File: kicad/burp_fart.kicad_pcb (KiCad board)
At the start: 2 copper layers, 142.2 x 120 mm, 44 parts

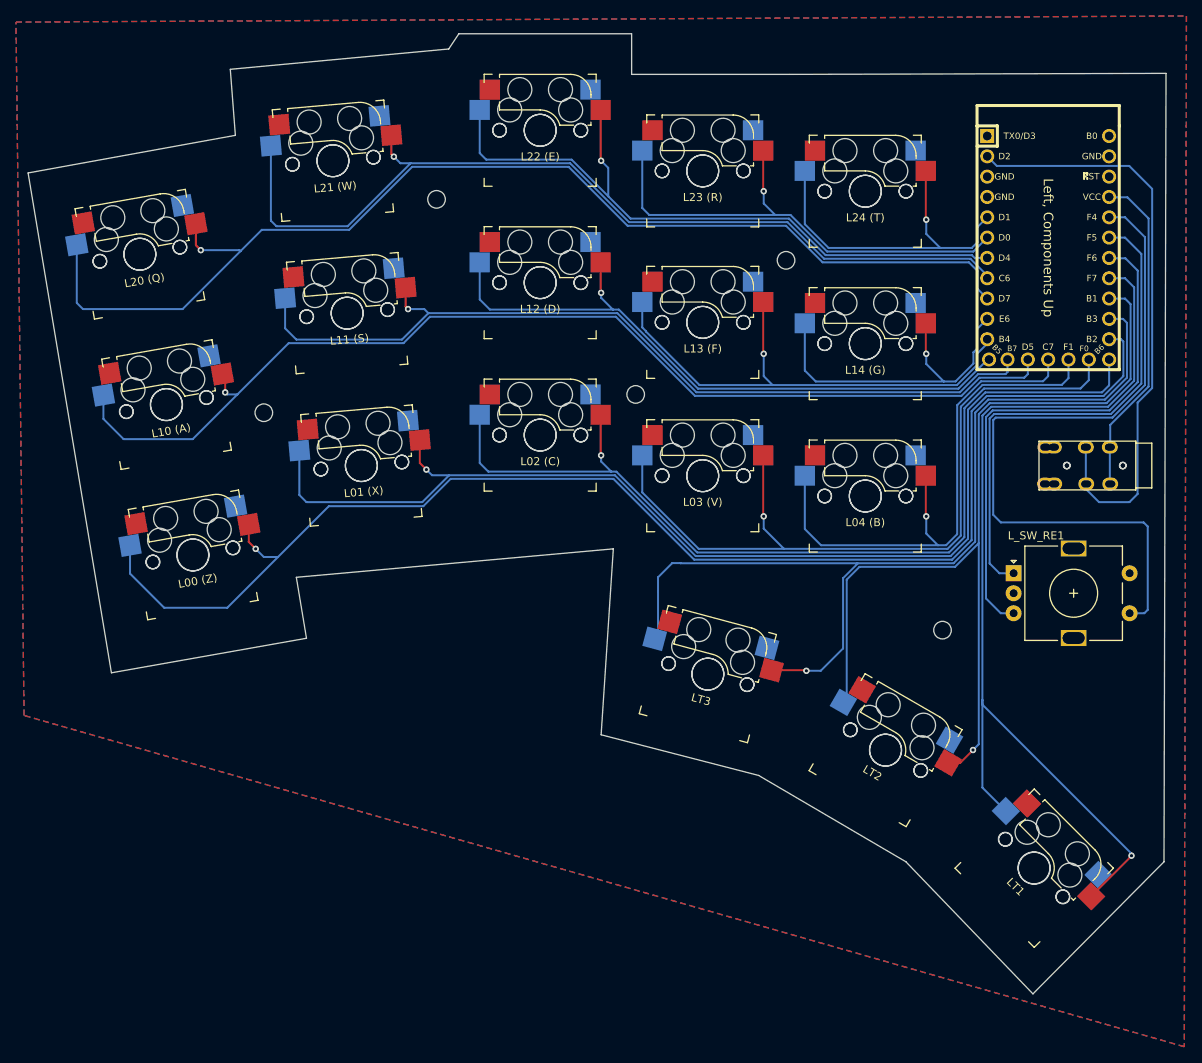
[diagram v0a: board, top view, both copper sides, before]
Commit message: update: makes edges rounded
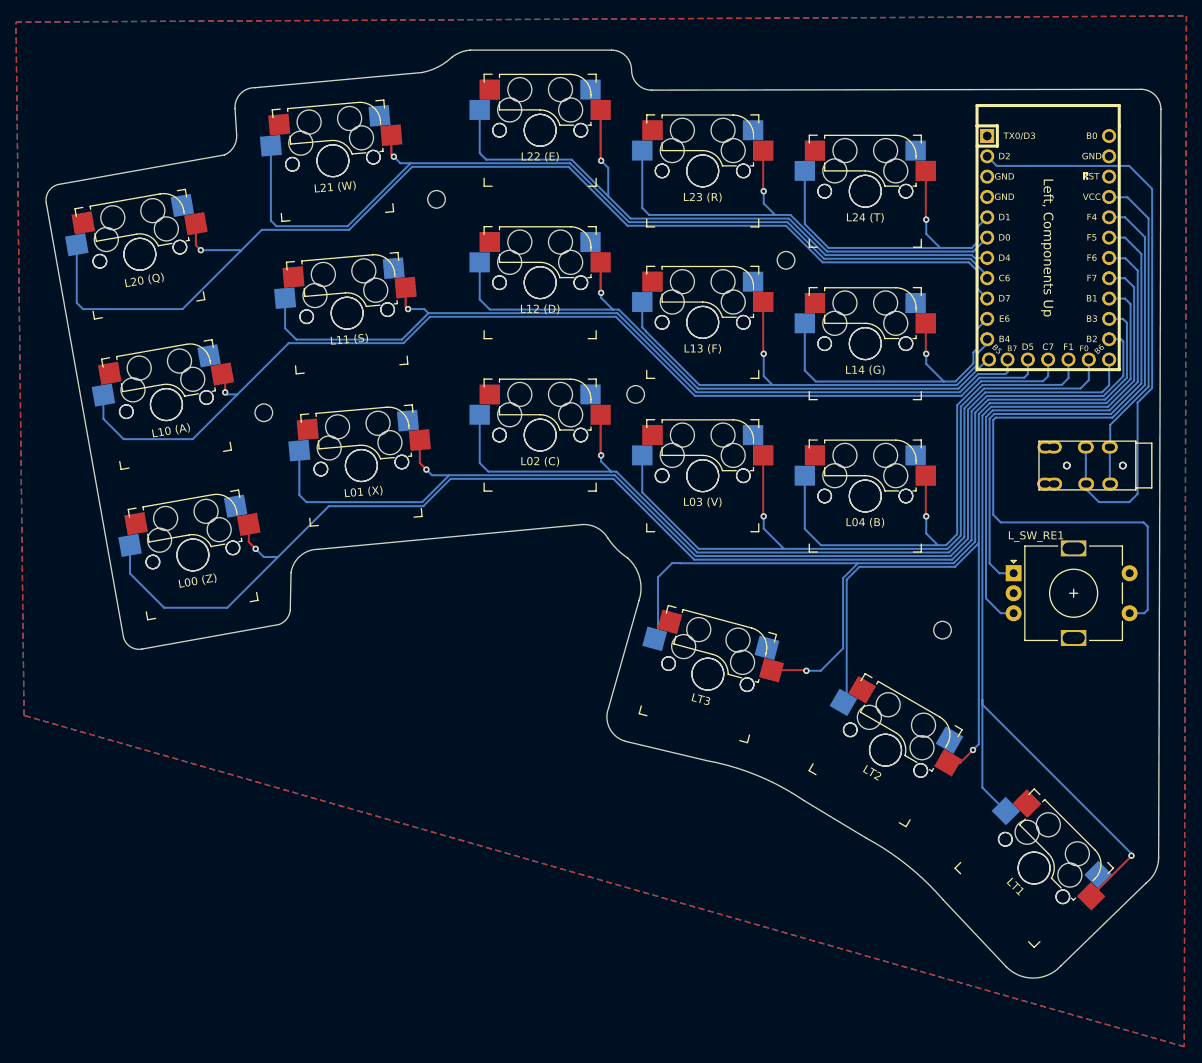
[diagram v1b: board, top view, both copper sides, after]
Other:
- board size 142.2 x 120 mm -> 139.4 x 116 mm
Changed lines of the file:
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@@
     (thickness 1.6)
   )
-  (paper "A3")
+  (paper "A4")
   (layers
     (0 "F.Cu" signal)
@@
       (layerselection 0x00010fc_ffffffff)
       (disableapertmacros false)
-      (usegerberextensions false)
+      (usegerberextensions true)
       (usegerberattributes true)
       (usegerberadvancedattributes true)
-      (creategerberjobfile true)
+      (creategerberjobfile false)
       (svguseinch false)
       (svgprecision 6)
@@
       (drillshape 0)
       (scaleselection 1)
-      (outputdirectory "gerbers/")
+      (outputdirectory "../gerbers/")
     )
   )
@@
     )
   )
-  (gr_line (start 86.36 108.585) (end 87.884 85.344) (layer "Edge.Cuts") (width 0.1))
-  (gr_line (start 48.26 88.9) (end 49.53 96.52) (layer "Edge.Cuts") (width 0.1))
-  (gr_line (start 67.31 22.86) (end 68.58 20.955) (layer "Edge.Cuts") (width 0.1))
-  (gr_line (start 140.335 140.97) (end 124.46 124.46) (layer "Edge.Cuts") (width 0.1))
-  (gr_line (start 40.005 25.4) (end 67.31 22.86) (layer "Edge.Cuts") (width 0.1))
-  (gr_line (start 49.53 96.52) (end 25.146 100.838) (layer "Edge.Cuts") (width 0.1))
-  (gr_line (start 90.17 20.955) (end 90.17 26.035) (layer "Edge.Cuts") (width 0.1))
-  (gr_line (start 40.64 33.655) (end 40.005 25.4) (layer "Edge.Cuts") (width 0.1))
-  (gr_line (start 68.58 20.955) (end 90.17 20.955) (layer "Edge.Cuts") (width 0.1))
-  (gr_line (start 90.17 26.035) (end 109.855 26.035) (layer "Edge.Cuts") (width 0.1))
-  (gr_line (start 14.732 38.354) (end 40.64 33.655) (layer "Edge.Cuts") (width 0.1))
-  (gr_line (start 156.972 25.908) (end 156.718 124.46) (layer "Edge.Cuts") (width 0.1))
-  (gr_line (start 25.146 100.838) (end 14.732 38.354) (layer "Edge.Cuts") (width 0.1))
-  (gr_line (start 87.884 85.344) (end 48.26 88.9) (layer "Edge.Cuts") (width 0.1))
-  (gr_line (start 156.718 124.46) (end 140.335 140.97) (layer "Edge.Cuts") (width 0.1))
-  (gr_line (start 106.045 113.665) (end 86.36 108.585) (layer "Edge.Cuts") (width 0.1))
-  (gr_line (start 124.46 124.46) (end 106.045 113.665) (layer "Edge.Cuts") (width 0.1))
-  (gr_line (start 156.972 25.908) (end 109.855 26.035) (layer "Edge.Cuts") (width 0.1))
+  (gr_arc (start 87.666742 23) (mid 89.434509 23.732233) (end 90.166742 25.5) (layer "Edge.Cuts") (width 0.1))
+  (gr_line (start 87.3 105.2) (end 91.1 91.8) (layer "Edge.Cuts") (width 0.1))
+  (gr_line (start 47.6 88.3) (end 47.5 93) (layer "Edge.Cuts") (width 0.1))
+  (gr_line (start 137.002391 137.579124) (end 129.1 129.2) (layer "Edge.Cuts") (width 0.1))
+  (gr_line (start 43.1 27.7) (end 64 25.8) (layer "Edge.Cuts") (width 0.1))
+  (gr_line (start 46.1 94.8) (end 28.952592 97.872693) (layer "Edge.Cuts") (width 0.1))
+  (gr_arc (start 153.837 27.9) (mid 155.604767 28.632233) (end 156.337 30.4) (layer "Edge.Cuts") (width 0.1))
+  (gr_line (start 40.8 33.6) (end 40.6 30.3) (layer "Edge.Cuts") (width 0.1))
+  (gr_arc (start 28.952592 97.872693) (mid 27.505304 97.578535) (end 26.652592 96.372693) (layer "Edge.Cuts") (width 0.1))
+  (gr_arc (start 92.670242 28.0035) (mid 90.9 27.270242) (end 90.166742 25.5) (layer "Edge.Cuts") (width 0.1))
+  (gr_arc (start 47.6 88.3) (mid 48.758903 86.21561) (end 51 85.4) (layer "Edge.Cuts") (width 0.1))
+  (gr_arc (start 17 42.1) (mid 17.294158 40.652712) (end 18.5 39.8) (layer "Edge.Cuts") (width 0.1))
+  (gr_arc (start 156.050253 123.923839) (mid 155.642005 125.69099) (end 154.5 127.1) (layer "Edge.Cuts") (width 0.1))
+  (gr_arc (start 89.4 109.4) (mid 87.414189 107.767908) (end 87.3 105.2) (layer "Edge.Cuts") (width 0.1))
+  (gr_arc (start 47.5 93) (mid 47.060729 94.102789) (end 46.1 94.8) (layer "Edge.Cuts") (width 0.1))
+  (gr_line (start 70 23) (end 87.666742 23) (layer "Edge.Cuts") (width 0.1))
+  (gr_arc (start 67.7 23.9) (mid 68.783048 23.278899) (end 70 23) (layer "Edge.Cuts") (width 0.1))
+  (gr_arc (start 99.5 111.8) (mid 105.862977 113.658335) (end 111.7 116.8) (layer "Edge.Cuts") (width 0.1))
+  (gr_line (start 18.5 39.8) (end 39.3 36.1) (layer "Edge.Cuts") (width 0.1))
+  (gr_line (start 156.337 30.4) (end 156.050253 123.923839) (layer "Edge.Cuts") (width 0.1))
+  (gr_arc (start 84.1 82.3) (mid 85.881729 82.727436) (end 87.2 84) (layer "Edge.Cuts") (width 0.1))
+  (gr_line (start 26.652592 96.372693) (end 17 42.1) (layer "Edge.Cuts") (width 0.1))
+  (gr_arc (start 40.8 33.6) (mid 40.439694 35.083817) (end 39.3 36.1) (layer "Edge.Cuts") (width 0.1))
+  (gr_arc (start 119.5 121.5) (mid 124.653436 124.909352) (end 129.1 129.2) (layer "Edge.Cuts") (width 0.1))
+  (gr_line (start 84.1 82.3) (end 51 85.4) (layer "Edge.Cuts") (width 0.1))
+  (gr_line (start 154.5 127.1) (end 143.8 137.5) (layer "Edge.Cuts") (width 0.1))
+  (gr_arc (start 143.8 137.5) (mid 140.418182 138.998881) (end 137.002391 137.579124) (layer "Edge.Cuts") (width 0.1))
+  (gr_line (start 99.5 111.8) (end 89.4 109.4) (layer "Edge.Cuts") (width 0.1))
+  (gr_line (start 119.5 121.5) (end 111.7 116.8) (layer "Edge.Cuts") (width 0.1))
+  (gr_arc (start 89.7 86.5) (mid 91.179059 88.944207) (end 91.1 91.8) (layer "Edge.Cuts") (width 0.1))
+  (gr_arc (start 40.6 30.3) (mid 41.277392 28.449415) (end 43.1 27.7) (layer "Edge.Cuts") (width 0.1))
+  (gr_arc (start 89.7 86.5) (mid 88.321525 85.378475) (end 87.2 84) (layer "Edge.Cuts") (width 0.1))
+  (gr_arc (start 67.7 23.9) (mid 65.982435 25.1079) (end 64 25.8) (layer "Edge.Cuts") (width 0.1))
+  (gr_line (start 153.837 27.9) (end 92.670242 28.0035) (layer "Edge.Cuts") (width 0.1))
   (segment (start 153.416 67.067168) (end 153.416 78.486) (width 0.25) (layer "B.Cu") (net 2))
   (segment (start 135.8213 37.47805) (end 152.37405 37.47805) (width 0.25) (layer "B.Cu") (net 2))
